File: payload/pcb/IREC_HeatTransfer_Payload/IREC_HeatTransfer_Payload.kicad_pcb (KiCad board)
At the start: 2 copper layers, 67.4 x 89.6 mm, 35 parts, among them J1 XT60PW-M, J2 Screw_Terminal_01x02, J3 Screw_Terminal_01x02, J4 Screw_Terminal_01x02, J5 Screw_Terminal_01x02, SW1 SW_SPDT, U1 MAX31855KASA, U2 DS18B20, U3 DEV-16771, U4 MAX31855KASA, U5 MAX31855KASA, U7 AP63357

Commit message: Updates
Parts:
- removed SW1: SW_SPDT, Button_Switch_SMD:SW_SPDT_CK_JS102011SAQN
- added G***: LOGO, Graphics:ARC_logo_black_13mm, F.Cu at (211.5, 102.8)
- added G***: LOGO, LOGO, F.Cu at (190.2, 103.1)
- added G***: LOGO, LOGO, F.Cu at (167.8, 102.3)
- added H1: MountingHole_Pad, MountingHole:MountingHole_2.2mm_M2_Pad_Via, F.Cu at (169.4, 35.3)
- added H2: MountingHole_Pad, MountingHole:MountingHole_2.2mm_M2_Pad_Via, F.Cu at (213.1, 35.3)
- added H3: MountingHole_Pad, MountingHole:MountingHole_2.2mm_M2_Pad_Via, F.Cu at (169.0, 130.3)
- added H4: MountingHole_Pad, MountingHole:MountingHole_2.2mm_M2_Pad_Via, F.Cu at (215.0, 130.0)
- R4: value R -> 22k
- R5: value R -> 93.1k
- moved U2 72.1 mm to (178.8, 93.8)
- moved J5 3.78 mm to (164.2, 65.2)
- moved U3 2.91 mm to (192.3, 116.9)
- moved J1 1.89 mm to (171.0, 48.2)
- moved J3 1.35 mm to (164.2, 73.9)
- moved J2 1.33 mm to (164.2, 82.6)
- moved C1 1.33 mm to (195.3, 96.8)
- moved C10 1.33 mm to (142.3, 68.7)
- moved C11 1.33 mm to (133.1, 73.3)
- moved C4 1.33 mm to (195.2, 84.2)
- moved C8 1.33 mm to (126.2, 79.1)
- moved C9 1.33 mm to (137.9, 68.7)
- moved J4 1.33 mm to (164.2, 91.3)
- moved R1 1.33 mm to (99.6, 68.2)
- moved R6 1.33 mm to (99.6, 82.9)
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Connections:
- net /DS_DATA renamed /TEMP_SENSE
- net /EN renamed Net-(U7-EN)
- U3 pad 15: unconnected-(U3-A1-Pad15) -> /VBAT_SENSE
- U3 pad 2: unconnected-(U3-OUT2-Pad2) -> /LED_RED
- U3 pad 3: unconnected-(U3-LRCLK2-Pad3) -> /LED_GREEN
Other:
- board size 67.4 x 89.6 mm -> 63.5 x 104.1 mm
- board text added: "+TC"
- board text added: "+TC1"
- board text added: "+TC2"
- board text added: "-TC1"
- board text added: "-TC2"
- board text added: "Designed By: Luca Beretta"

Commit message: updates to pcb
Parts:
- removed TC1, TC2, TC3: Thermocouple_Block, CustomFootprintLib:PCC-SMP-K
- added D1: OSRAM_LGR971-KN-1, Skyhawkson_Footprints:OSRAM_0805, F.Cu at (163.3, 101.1)
- added D2: OSRAM_LSR976-NR-1, Skyhawkson_Footprints:OSRAM_0805, F.Cu at (163.3, 98.0)
- C1, C2, C3, C4, C5, C6: moved to B.Cu
- H1, H2, H3, H4: footprint MountingHole:MountingHole_2.2mm_M2_Pad_Via -> MountingHole:MountingHole_3.2mm_M3_Pad_Via
- J5: value Screw_Terminal_01x02 -> S2B-PH-K-SLFSN; footprint CustomFootprintLib:TERMBLOCK_OSTTE020104_3_5MM -> CustomFootprintLib:CONN_S2B-PH-K-S_JST
- moved J1 39.8 mm to (170.9, 88.0)
- moved J4 39.5 mm to (181.8, 55.9), turned to 180 degrees
- moved J3 39.3 mm to (199.2, 55.9), turned to 180 degrees
- moved G*** 38.4 mm to (220.0, 78.7), turned to 90 degrees
- moved J2 37.5 mm to (190.5, 55.9), turned to 180 degrees
- moved R4 36.4 mm to (213.6, 86.5)
- moved R5 36.4 mm to (213.6, 89.4)
- moved C1 31.3 mm to (199.4, 65.8), turned to 0 degrees
- moved G*** 28.9 mm to (180.6, 128.3)
- moved C6 27.9 mm to (181.9, 68.3), turned to 0 degrees
- moved G*** 26.0 mm to (204.0, 127.8)
- moved U5 22.6 mm to (181.9, 68.3), turned to -90 degrees
- moved U1 22.6 mm to (199.4, 68.3), turned to -90 degrees
- moved H2 22.3 mm to (215.8, 57.4)
- moved H1 22.1 mm to (168.3, 57.4)
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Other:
- board size 63.5 x 104.1 mm -> 63.5 x 83.8 mm
- board text added: "+TC3"
- board text added: "-TC3"
- board text added: "Designed by Luca Beretta"
- board text removed: "+TC"
- board text removed: "Designed By: Luca Beretta"

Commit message: updates
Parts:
- removed J2, J3, J4: Screw_Terminal_01x02, CustomFootprintLib:TERMBLOCK_OSTTE020104_3_5MM
- removed R8: 5, Resistor_SMD:R_0805_2012Metric_Pad1.20x1.40mm_HandSolder
- added BT1: Battery_Cell, Battery:BatteryHolder_Keystone_3002_1x2032, B.Cu at (184.1, 60.7)
- added J6: Screw_Terminal_01x02, CustomFootprintLib:TERMBLOCK_OSTTE020104_3_5MM, F.Cu at (156.7, 67.5)
- added SW1: SW_Push_SPDT, Button_Switch_SMD:SW_SPDT_CK_JS102011SAQN, F.Cu at (154.7, 96.5)
- added TP1: +5V, TestPoint:TestPoint_Keystone_5019_Minature, F.Cu at (181.1, 101.1)
- added TP2: VIN, TestPoint:TestPoint_Keystone_5019_Minature, F.Cu at (163.1, 91.9)
- added TP3: GND, TestPoint:TestPoint_Keystone_5019_Minature, F.Cu at (213.4, 63.8)
- J5: value S2B-PH-K-SLFSN -> Screw_Terminal_01x06; footprint CustomFootprintLib:CONN_S2B-PH-K-S_JST -> CustomFootprintLib:TERMBLOCK_OSTTE060104
- R1, R4, R5: moved to B.Cu
- R6: value 75 -> R; moved to B.Cu
- R7: value 5 -> R; moved to B.Cu
- moved R7 107.4 mm to (206.0, 100.6)
- moved R6 107.4 mm to (206.0, 97.4), turned to 180 degrees
- moved R1 101.8 mm to (184.4, 124.5)
- moved R5 57.3 mm to (157.5, 78.2), turned to 90 degrees
- moved C8 56.2 mm to (182.4, 81.7), turned to 180 degrees
- moved C11 55.6 mm to (187.0, 87.0), turned to -90 degrees
- moved C9 54.2 mm to (187.0, 91.9), turned to 90 degrees
- moved R2 54.1 mm to (182.4, 84.0), turned to 180 degrees
- moved R3 53.2 mm to (179.1, 82.7)
- moved R4 52.8 mm to (162.1, 97.8), turned to 90 degrees
- moved C10 52.5 mm to (187.0, 96.2), turned to -90 degrees
- moved U7 50.9 mm to (183.1, 87.1), turned to 180 degrees
- moved D1 49.9 mm to (213.1, 97.5), turned to 0 degrees
- moved D2 49.9 mm to (213.1, 100.6), turned to 0 degrees
- moved L1 45.4 mm to (181.1, 94.1), turned to -90 degrees
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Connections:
- C4 pad 1: Net-(J3-Pin_2) -> /+TC1
- C4 pad 2: Net-(J3-Pin_1) -> /-TC1
- C5 pad 1: Net-(J2-Pin_2) -> /+TC2
- C5 pad 2: Net-(J2-Pin_1) -> /-TC2
- C6 pad 1: Net-(J4-Pin_2) -> /+TC3
- C6 pad 2: Net-(J4-Pin_1) -> /-TC3
- J5 pad 1: +BATT -> /+TC3
- J5 pad 2: GND -> /-TC3
- R4 pad 2: Net-(U7-EN) -> /EN
- R5 pad 1: Net-(U7-EN) -> Net-(SW1-A)
- R6 pad 1: /RED -> Net-(D1-PadA)
- R6 pad 2: Net-(D1-RED) -> /LED_GREEN
- R7 pad 1: /BLU -> /LED_RED
- R7 pad 2: Net-(D1-BLU) -> Net-(D2-PadA)
- U1 pad 2: Net-(J3-Pin_1) -> /-TC1
- U1 pad 3: Net-(J3-Pin_2) -> /+TC1
- U3 pad VBAT: unconnected-(U3-PadVBAT) -> /VBAT_CR2032
- U4 pad 2: Net-(J2-Pin_1) -> /-TC2
- U4 pad 3: Net-(J2-Pin_2) -> /+TC2
- U5 pad 2: Net-(J4-Pin_1) -> /-TC3
- U5 pad 3: Net-(J4-Pin_2) -> /+TC3
- U7 pad 2: Net-(U7-EN) -> /EN
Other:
- board text added: "+5V"
- board text added: "+VCC"
- board text added: "Heat Transfer Board - Perception"
- board text added: "I"
- board text added: "O"

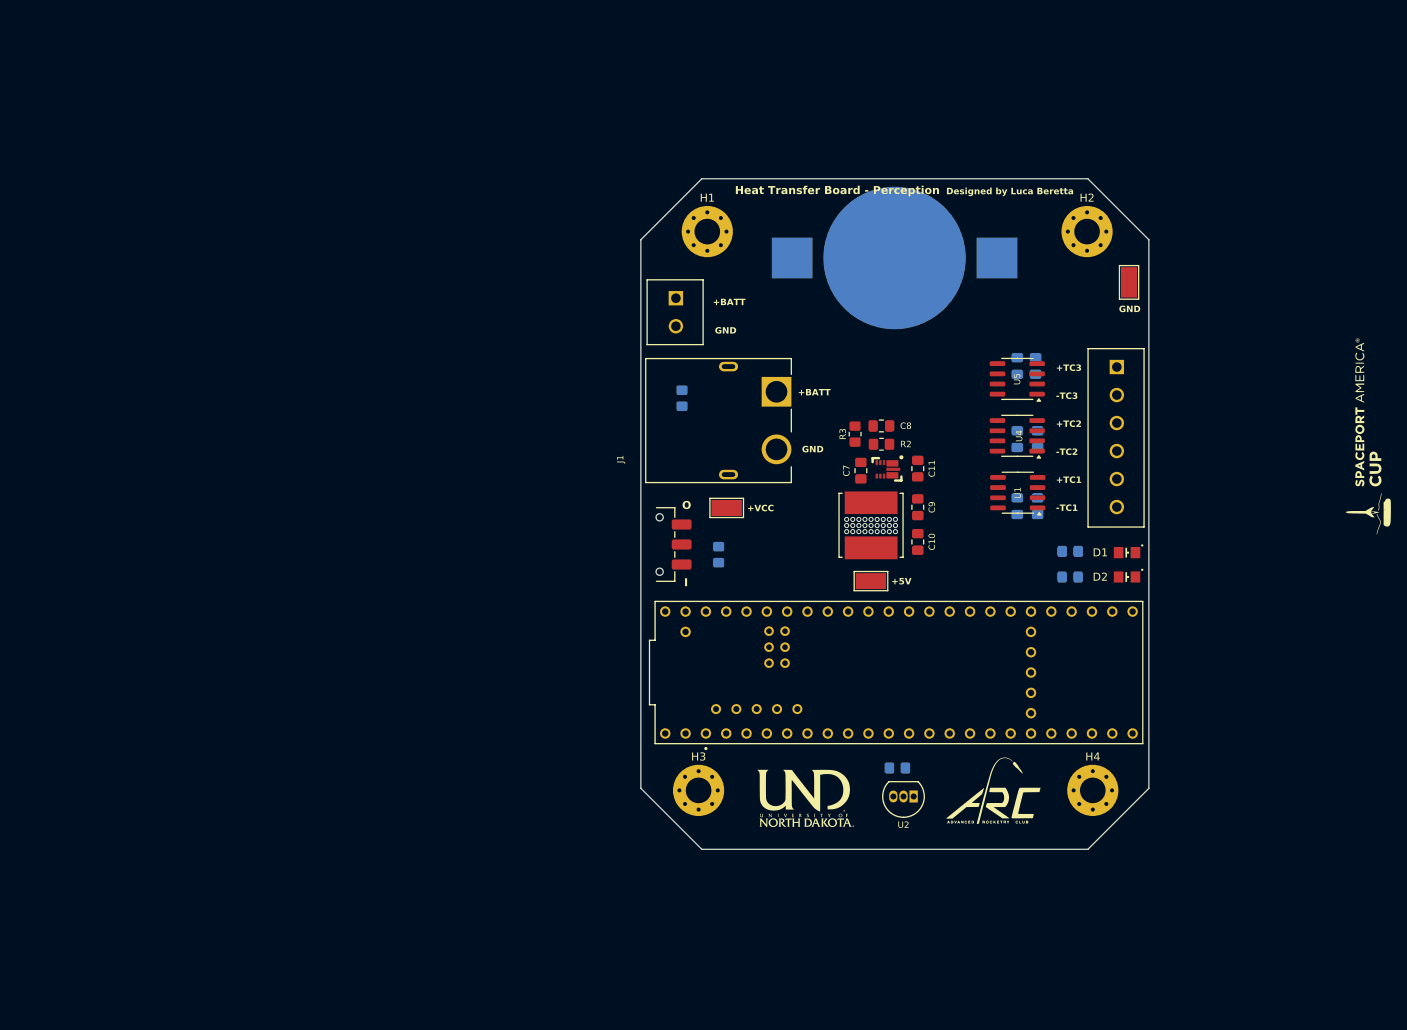
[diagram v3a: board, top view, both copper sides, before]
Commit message: updates
continued buck layout
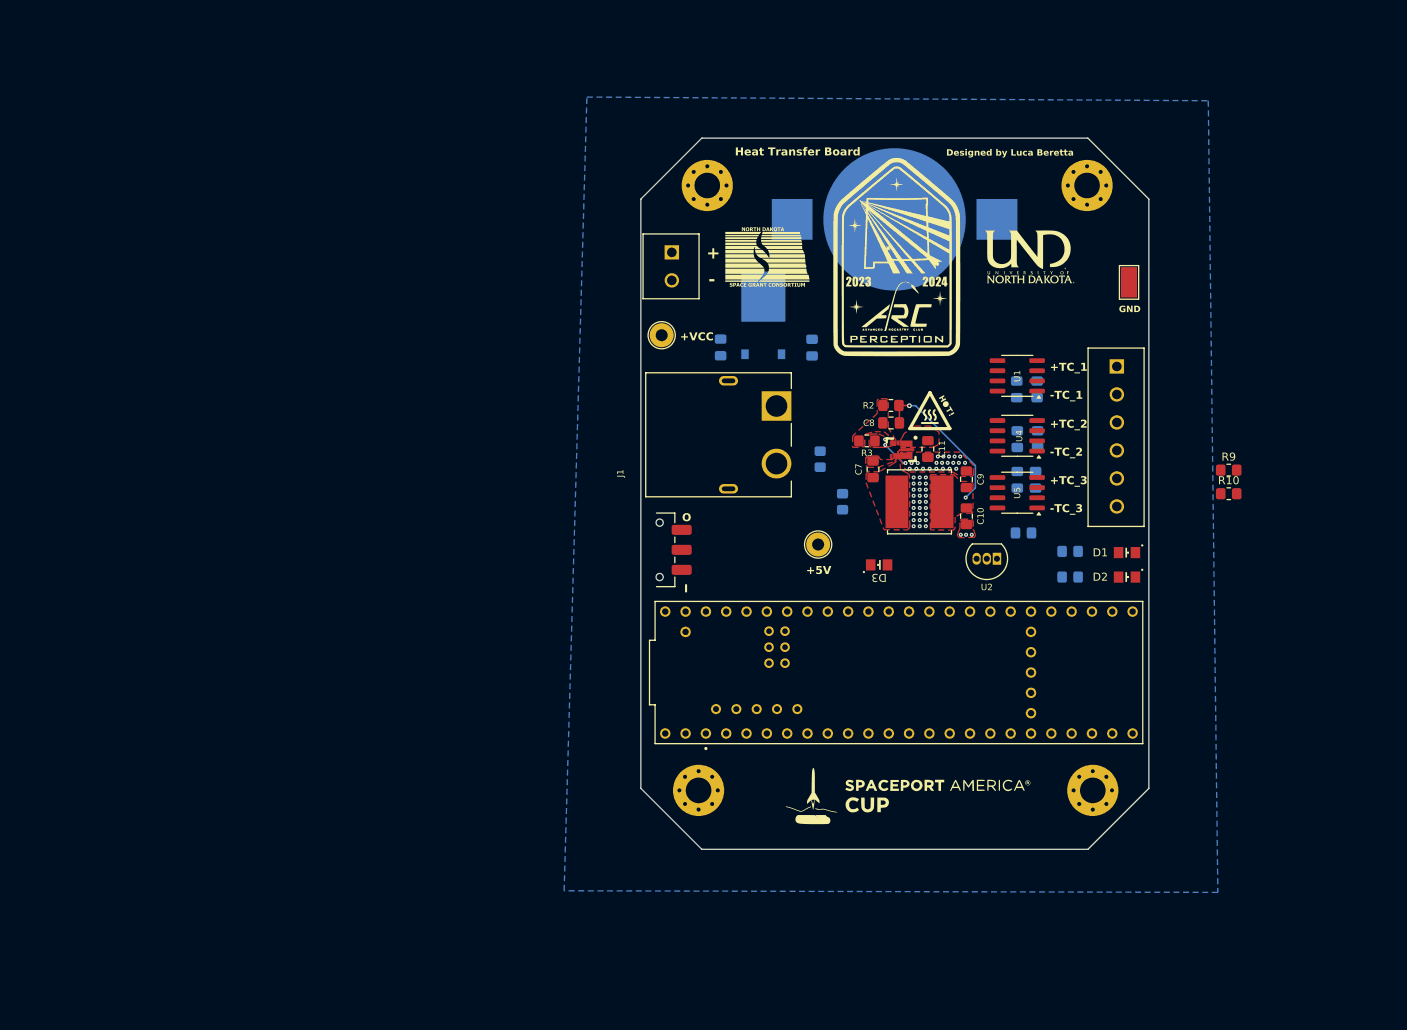
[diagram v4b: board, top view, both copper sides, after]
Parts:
- removed the G*** at (196.3, 127.8)
- added C14: 0.33uF, Capacitor_SMD:C_0805_2012Metric_Pad1.18x1.45mm_HandSolder, B.Cu at (173.7, 71.9)
- added C15: 0.1uF, Capacitor_SMD:C_0805_2012Metric_Pad1.18x1.45mm_HandSolder, B.Cu at (162.3, 71.9)
- added D3: OSRAM_LGR971-KN-1, Skyhawkson_Footprints:OSRAM_0805, F.Cu at (182.1, 99.1)
- added G***: LOGO, LOGO, F.Cu at (168.1, 60.6)
- added G1: LOGO, LOGO, F.Cu at (184.4, 60.5)
- added R10: 100k, Resistor_SMD:R_0805_2012Metric_Pad1.20x1.40mm_HandSolder, F.Cu at (225.8, 90.2)
- added R9: 200k, Resistor_SMD:R_0805_2012Metric_Pad1.20x1.40mm_HandSolder, F.Cu at (225.8, 87.2)
- added U$10: , SparkFun_Buck_Regulator_AP63357DV-7_BabyBuck5V:HOT##7, F.Cu at (190.6, 79.2)
- added U$8: , SparkFun_Buck_Regulator_AP63357DV-7_BabyBuck5V:HIGH_TEMP_WARNING, F.Cu at (188.5, 80.4)
- added U8: NJM7805SDL1-TE1, CustomFootprintLib:TO-252-3-L1_NMD, B.Cu at (167.6, 66.9)
- TP1, TP2: footprint TestPoint:TestPoint_Keystone_5019_Minature -> TestPoint:TestPoint_Loop_D2.54mm_Drill1.5mm_Beaded
- moved G*** 73.2 mm to (200.9, 60.6)
- moved G*** 73.1 mm to (185.7, 128.0), turned to 0 degrees
- moved R1 33.3 mm to (200.2, 95.1)
- moved U2 31.5 mm to (196.8, 98.3)
- moved TP2 23.1 mm to (154.9, 70.4), turned to 90 degrees
- moved R5 18.9 mm to (174.8, 85.9), turned to -90 degrees
- moved R4 16.8 mm to (177.5, 91.2)
- moved C1 14.6 mm to (201.9, 77.1)
- moved C4 14.6 mm to (199.3, 77.1)
- moved U1 14.6 mm to (199.4, 75.4)
- moved C3 14.2 mm to (201.7, 88.4)
- moved C6 14.2 mm to (199.4, 88.4)
- moved U5 14.2 mm to (199.4, 90.0)
- moved TP1 8.03 mm to (174.5, 96.5), turned to 90 degrees
- moved C9 7.01 mm to (193.0, 88.4)
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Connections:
- J5 pad 1: /+TC3 -> /+TC1
- J5 pad 2: /-TC3 -> /-TC1
- J5 pad 5: /+TC1 -> /+TC3
- J5 pad 6: /-TC1 -> /-TC3
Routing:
- net +5V: track 0.00 -> 19.4 mm, vias 0 -> 2
- net GND: track 0.00 -> 3.48 mm, vias 27 -> 54
- net Net-(U7-SW): track 0.00 -> 1.87 mm
- added copper zone on F.Cu, net +5V
- added copper zone on F.Cu, net +BATT
- added copper zone on B.Cu, net GND
- added copper zone on F.Cu, net GND
- added copper zone on F.Cu, net Net-(U7-BST)
- added copper zone on F.Cu, net Net-(U7-FB)
- added copper zone on F.Cu, net Net-(U7-SW)
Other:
- board size 63.5 x 83.8 mm -> 63.5 x 88.9 mm
- board text added: "+"
- board text added: "+TC_1"
- board text added: "+TC_2"
- board text added: "+TC_3"
- board text added: "-"
- board text added: "-TC_1"
- board text added: "-TC_2"
- board text added: "-TC_3"
- board text added: "Heat Transfer Board"
- board text removed: "+BATT"
- board text removed: "+TC1"
- board text removed: "+TC2"
- board text removed: "+TC3"
- board text removed: "-TC1"
- board text removed: "-TC2"
- board text removed: "-TC3"
- board text removed: "Heat Transfer Board - Perception"

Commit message: updates
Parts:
- removed D3: OSRAM_LGR971-KN-1, Skyhawkson_Footprints:OSRAM_0805
- removed U$10: , SparkFun_Buck_Regulator_AP63357DV-7_BabyBuck5V:HOT##7
- removed U$8: , SparkFun_Buck_Regulator_AP63357DV-7_BabyBuck5V:HIGH_TEMP_WARNING
- R7: moved to F.Cu
- TP1, TP2: footprint TestPoint:TestPoint_Loop_D2.54mm_Drill1.5mm_Beaded -> TestPoint:TestPoint_Pad_D1.0mm
- TP3: footprint TestPoint:TestPoint_Keystone_5019_Minature -> TestPoint:TestPoint_Pad_D1.0mm
- moved TP3 53.4 mm to (173.1, 98.8)
- moved TP2 30.4 mm to (165.7, 98.8)
- moved D2 25.6 mm to (191.5, 86.9), turned to 90 degrees
- moved R7 17.1 mm to (191.5, 91.4), turned to 90 degrees
- moved R4 15.6 mm to (163.8, 98.6), turned to 180 degrees
- moved R5 14.7 mm to (163.8, 95.8), turned to 0 degrees
- moved J6 7.85 mm to (156.5, 69.6)
- moved TP1 5.57 mm to (169.4, 98.8)
- moved R6 4.81 mm to (210.1, 99.9)
- moved C10 4.10 mm to (189.2, 91.5)
- moved C7 4.10 mm to (177.5, 85.6)
- moved C8 4.10 mm to (179.8, 79.8)
- moved C9 4.10 mm to (189.2, 86.8)
- moved L1 4.10 mm to (183.4, 89.7)
- moved R2 4.10 mm to (179.8, 77.6)
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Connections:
- R7 pad 1: /LED_RED -> +5V
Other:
- board text added: "${REFERENCE}"
- board text added: "5V"
- board text added: "VCC"
- board text removed: "+5V"
- board text removed: "+VCC"

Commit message: updates
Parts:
- removed J6: Screw_Terminal_01x02, CustomFootprintLib:TERMBLOCK_OSTTE020104_3_5MM
- removed R5: 93.1k, Resistor_SMD:R_0805_2012Metric_Pad1.20x1.40mm_HandSolder
- removed SW1: SW_Push_SPDT, Button_Switch_SMD:SW_SPDT_CK_JS102011SAQN
- added J4: Screw_Terminal_01x06, CustomFootprintLib:TERMBLOCK_OSTTE060104, F.Cu at (156.6, 64.8)
- added JP1: Jumper_3_Open, Jumper:SolderJumper-3_P1.3mm_Open_RoundedPad1.0x1.5mm, F.Cu at (169.2, 75.9)
- added U$10: , SparkFun_Buck_Regulator_AP63357DV-7_BabyBuck5V:HOT##7, F.Cu at (190.8, 82.5)
- added U$8: , SparkFun_Buck_Regulator_AP63357DV-7_BabyBuck5V:HIGH_TEMP_WARNING, F.Cu at (188.7, 83.8)
- R4: value 22k -> R; moved to F.Cu
- moved R4 51.4 mm to (130.4, 59.5), turned to -90 degrees
- moved G*** 42.2 mm to (127.6, 72.1)
- moved TP1 27.0 mm to (183.8, 75.9)
- moved TP2 27.0 mm to (180.1, 75.9)
- moved TP3 27.0 mm to (187.5, 75.9)
- moved C15 12.0 mm to (172.5, 78.3)
- moved J1 11.2 mm to (163.3, 94.0)
- moved U2 3.56 mm to (200.4, 98.3)
- moved R2 2.59 mm to (179.3, 80.2)
- moved U7 2.59 mm to (180.6, 85.7)
- moved C7 2.59 mm to (177.0, 88.1)
- moved C8 2.59 mm to (179.3, 82.3)
- moved D2 2.59 mm to (191.0, 89.4)
- moved R7 2.59 mm to (191.0, 94.0)
- moved C11 2.59 mm to (183.9, 85.6)
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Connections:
- net /+TC1 renamed /T1
- net /+TC2 renamed /T2
- net /+TC3 renamed /T3
- net /TC1_CS renamed /T1_CS
- net /TC2_CS renamed /T2_CS
- net /TC3_CS renamed /T3_CS
- C11 pad 1: +BATT -> V_BUCK
- C14 pad 1: +BATT -> V_LDO
- C4 pad 2: /-TC1 -> /T-
- C5 pad 2: /-TC2 -> /T-
- C6 pad 2: /-TC3 -> /T-
- J5 pad 2: /-TC1 -> /T-
- J5 pad 4: /-TC2 -> /T-
- J5 pad 6: /-TC3 -> /T-
- R4 pad 1: GND -> Net-(J4-Pin_5)
- R4 pad 2: /EN -> /LED_GREEN
- R9 pad 1: +BATT -> VCC
- TP2 pad 1: +BATT -> V_BUCK
- U1 pad 2: /-TC1 -> /T-
- U3 pad 3.3V_1: unconnected-(U3-3.3V-Pad3.3V_1) -> +3V3
- U4 pad 2: /-TC2 -> /T-
- U5 pad 2: /-TC3 -> /T-
- U7 pad 1: +BATT -> V_BUCK
- U7 pad 2: /EN -> V_BUCK
- U8 pad 1: +BATT -> V_LDO
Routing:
- added copper zone on F.Cu, net V_BUCK
- removed copper zone on F.Cu, net +BATT
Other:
- board text added: "BATT+"
- board text added: "BATT-"
- board text added: "BUCK"
- board text added: "LDO"
- board text added: "LED+"
- board text added: "LED-"
- board text added: "SW+"
- board text added: "SW-"
- board text added: "TC1+"
- board text added: "TC1-"
- board text added: "TC2+"
- board text added: "TC2-"
- board text added: "TC3+"
- board text added: "TC3-"
- board text removed: "+"
- board text removed: "+TC_1"
- board text removed: "+TC_2"
- board text removed: "+TC_3"
- board text removed: "-"
- board text removed: "-TC_1"
- board text removed: "-TC_2"
- board text removed: "-TC_3"
- board text removed: "I"
- board text removed: "O"

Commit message: upd
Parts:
- removed U$10: , SparkFun_Buck_Regulator_AP63357DV-7_BabyBuck5V:HOT##7
- removed U$8: , SparkFun_Buck_Regulator_AP63357DV-7_BabyBuck5V:HIGH_TEMP_WARNING
- added J4: Conn_01x04, Connector_PinSocket_2.54mm:PinSocket_1x04_P2.54mm_Vertical, F.Cu at (156.0, 124.5)
- added J5: GPIO, Connector_PinSocket_2.54mm:PinSocket_1x04_P2.54mm_Vertical, F.Cu at (212.9, 125.0)
- added J6: SPI, Connector_PinSocket_2.54mm:PinSocket_1x03_P2.54mm_Vertical, F.Cu at (194.1, 126.5)
- added J7: I2C, Connector_PinSocket_2.54mm:PinSocket_1x02_P2.54mm_Vertical, F.Cu at (175.8, 127.3)
- added TP3: VIN, TestPoint:TestPoint_Pad_D1.0mm, F.Cu at (234.9, 108.0)
- TP2: value VIN -> +5V
- moved H3 12.9 mm to (159.6, 140.1)
- moved H4 12.9 mm to (208.8, 140.1)
- moved G*** 11.7 mm to (184.7, 139.7)
- renumbered C4 to C1, C14 to C10, C9 to C11, C10 to C12, C15 to C13, C5 to C2, C6 to C3, C11 to C4, C1 to C5, C2 to C6, C3 to C7, C7 to C8, C8 to C9, D2 to D1, D1 to D2, J5 to J1, J1 to J2, J4 to J3, R7 to R1, R6 to R2, R1 to R3, R2 to R4, R3 to R5, R4 to R6, R9 to R7, R10 to R8, TP3 to TP1, TP1 to TP2, U4 to U2, U5 to U3, U7 to U4, U2 to U5, U8 to U6, U3 to U7
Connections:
- TP2 pad 1: V_BUCK -> +5V
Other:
- board size 63.5 x 88.9 mm -> 63.5 x 101.6 mm

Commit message: upd
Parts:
- added JP2: Jumper_2_Open, CustomFootprintLib:SolderJumper, B.Cu at (200.7, 140.2)
- J4: value Conn_01x04 -> POWER
- moved H1 1.81 mm to (160.0, 53.3)
- moved D2 0.97 mm to (212.3, 99.8)
- moved H2 0.94 mm to (208.2, 52.6)
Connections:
- H1 pad 1: GND -> unconnected-(H1-Pad1)
- H2 pad 1: GND -> unconnected-(H2-Pad1)_7
- H3 pad 1: GND -> unconnected-(H3-Pad1)_0
- H4 pad 1: GND -> Net-(JP2-A)
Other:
- outline, holes or cut-outs redrawn
- board text added: "3V3"
- board text added: "GND Mounting Hole"
- board text added: "GPIO"
- board text added: "MISO"
- board text added: "MOSI"
- board text added: "SCK"
- board text added: "SCL"
- board text added: "SDA"
- board text added: "STATUS"
